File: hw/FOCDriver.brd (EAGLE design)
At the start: 82.5 x 57.8 mm, 99 parts, among them U1 IX4428N, U2 IX4428N, U3 IX4428N, U4 IRF9389TRPBF, U5 IRF9389TRPBF, U6 IRF9389TRPBF, U7 LM27313XMF, U8 LM358N, U9 LM358N

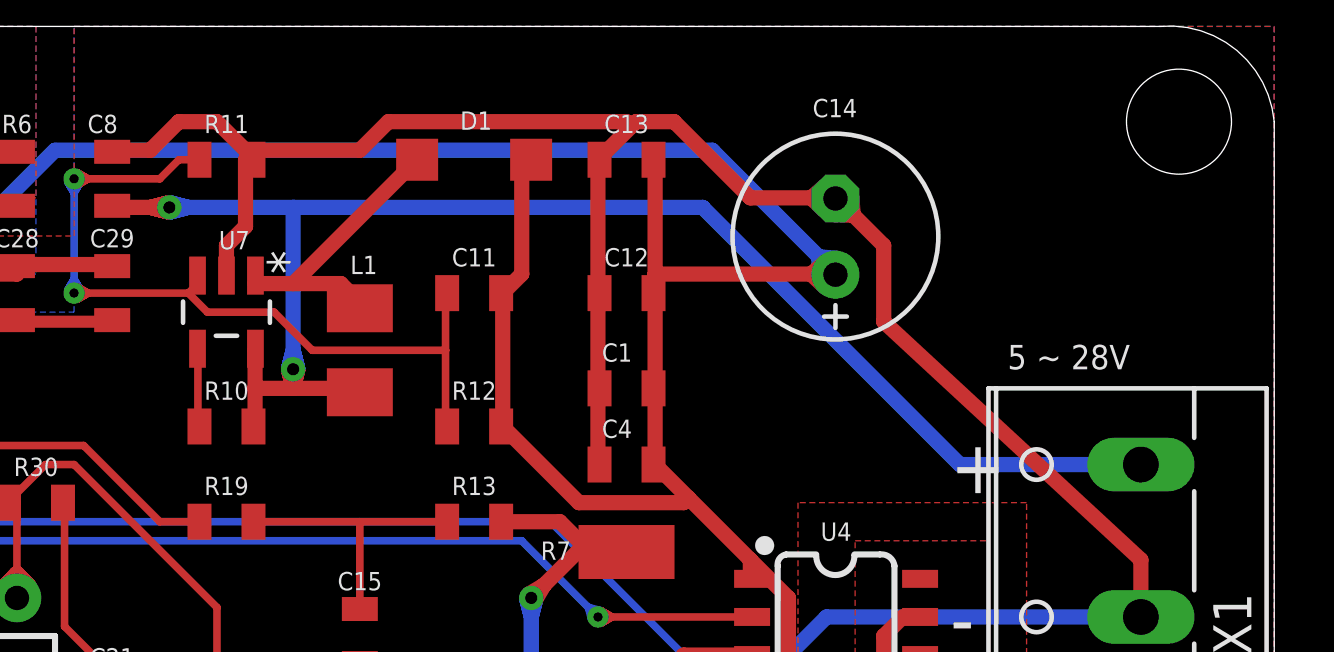
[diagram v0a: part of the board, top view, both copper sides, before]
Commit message: add resettable fuse
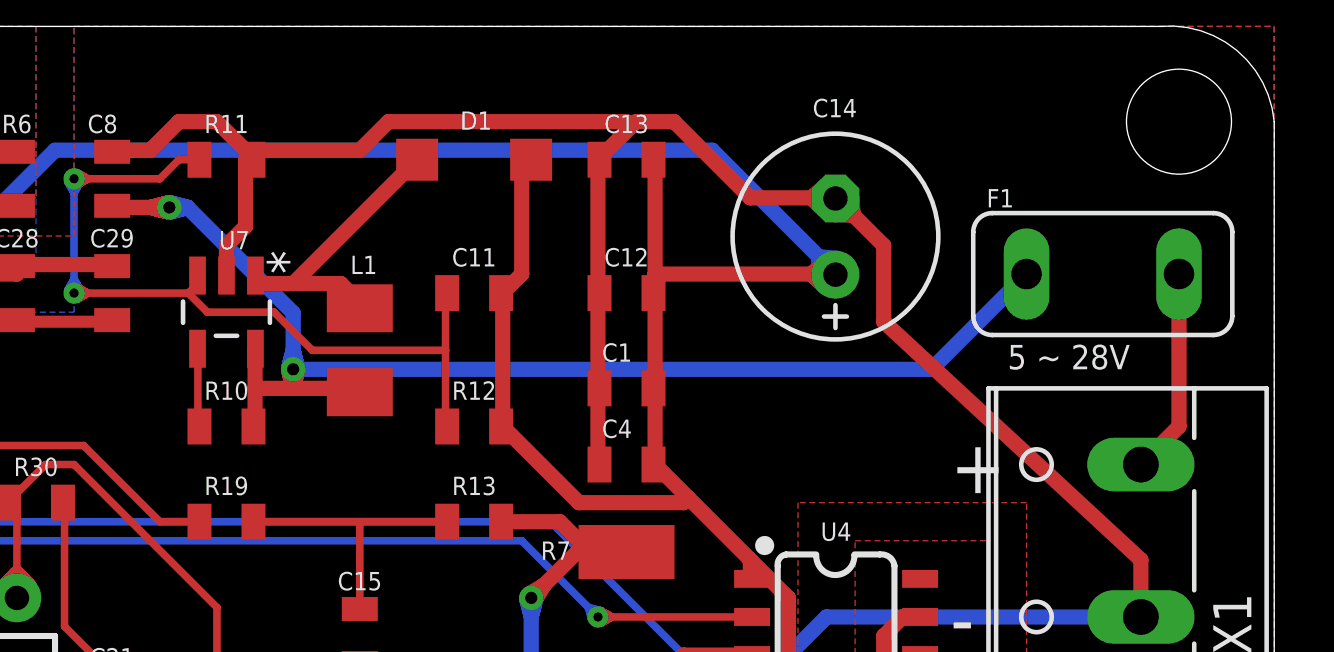
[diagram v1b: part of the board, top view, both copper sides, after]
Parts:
- added F1: 4.00A 16V, fuse:TE5
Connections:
- new net N$27: F1.1, X1.2
- net N$1: now also F1.2; no longer X1.2
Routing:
- net N$1: track 77.5 -> 69.4 mm
- net N$27: track 0.00 -> 6.88 mm
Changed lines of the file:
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@@
 <attribute name="VALUE" x="8.763" y="55.3466" size="1.27" layer="27" ratio="10" rot="R270"/>
 </element>
+<element name="F1" library="fuse" package="TE5" value="4.00A 16V" x="76.835" y="50.8" smashed="yes" rot="R180">
+<attribute name="OC_FARNELL" value="unknown" x="76.835" y="50.8" size="1.778" layer="27" rot="R180" display="off"/>
+<attribute name="MPN" value="" x="76.835" y="50.8" size="1.778" layer="27" rot="R180" display="off"/>
+<attribute name="OC_NEWARK" value="unknown" x="76.835" y="50.8" size="1.778" layer="27" rot="R180" display="off"/>
+<attribute name="MF" value="" x="76.835" y="50.8" size="1.778" layer="27" rot="R180" display="off"/>
+<attribute name="NAME" x="72.9615" y="53.0225" size="0.6096" layer="25" ratio="20"/>
+<attribute name="VALUE" x="81.153" y="54.61" size="1.27" layer="27" ratio="10" rot="R180"/>
+</element>
 </elements>
 <signals>
@@
 <wire x1="45.72" y1="53.0225" x2="45.1104" y2="53.0225" width="0.508" layer="1"/>
 <wire x1="45.1104" y1="53.0225" x2="43.815" y2="53.0225" width="0.508" layer="1"/>
-<wire x1="63.5" y1="53.0225" x2="49.8475" y2="53.0225" width="0.508" layer="16"/>
-<wire x1="49.8475" y1="53.0225" x2="46.3296" y2="53.0225" width="0.508" layer="16"/>
+<wire x1="46.3296" y1="53.0225" x2="49.8475" y2="49.5046" width="0.508" layer="16"/>
+<wire x1="49.8475" y1="49.5046" x2="49.8475" y2="48.2346" width="0.508" layer="16"/>
 <wire x1="46.3296" y1="53.0225" x2="45.72" y2="53.0225" width="0.508" layer="16"/>
-<wire x1="72.0725" y1="44.45" x2="63.5" y2="53.0225" width="0.508" layer="16"/>
-<wire x1="78.105" y1="44.45" x2="72.0725" y2="44.45" width="0.508" layer="16"/>
 <wire x1="43.815" y1="53.0225" x2="43.815" y2="53.075" width="0.508" layer="1"/>
 <wire x1="49.8475" y1="47.625" x2="49.8475" y2="47.0154" width="0.508" layer="1"/>
 <wire x1="49.8475" y1="47.0154" x2="49.8475" y2="46.99" width="0.508" layer="1"/>
-<wire x1="49.8475" y1="53.0225" x2="49.8475" y2="48.2346" width="0.508" layer="16"/>
 <via x="45.72" y="53.0225" extent="1-16" drill="0.4064"/>
 <via x="49.8475" y="47.625" extent="1-16" drill="0.4064"/>
@@
 <wire x1="49.847496875" y1="48.2346" x2="49.6999375" y2="47.663103125" width="0.508" layer="16"/>
 <wire x1="49.6999375" y1="47.663103125" x2="49.6999375" y2="47.6631" width="0.508" layer="16"/>
-<contactref element="X1" pad="2"/>
 <wire x1="45.68189375" y1="52.8749375" x2="45.681896875" y2="52.8749375" width="0.508" layer="1"/>
 <wire x1="46.3296" y1="53.0225" x2="45.758103125" y2="53.170059375" width="0.508" layer="16"/>
@@
 <wire x1="49.847496875" y1="48.2346" x2="49.995059375" y2="47.6631" width="0.508" layer="16"/>
 <wire x1="49.8475" y1="47.625" x2="49.995059375" y2="47.6631" width="0.508" layer="16"/>
+<contactref element="F1" pad="2"/>
+<wire x1="74.295" y1="50.8" x2="71.12" y2="47.625" width="0.508" layer="16"/>
+<wire x1="71.12" y1="47.625" x2="49.8475" y2="47.625" width="0.508" layer="16"/>
 </signal>
 <signal name="N$2">
@@
 <wire x1="3.81" y1="43.815" x2="3.7795375" y2="43.129875" width="0.508" layer="1"/>
 </signal>
+<signal name="N$27" class="3">
+<contactref element="X1" pad="2"/>
+<contactref element="F1" pad="1"/>
+<wire x1="78.105" y1="44.45" x2="79.375" y2="45.72" width="0.508" layer="1"/>
+<wire x1="79.375" y1="45.72" x2="79.375" y2="50.8" width="0.508" layer="1"/>
+</signal>
 </signals>

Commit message: trans
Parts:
- removed C10: 0.1uF, SparkFun-Capacitors:0805
- removed U1, U2, U3: IX4428N, IX4428N:SO08
- added Q1, Q2, Q3, Q4, Q5, Q6: BC546B, transistor-npn:TO92-EBC
- added R47, R50: 330, SparkFun-Resistors:0805
- added R48, R51: 180, SparkFun-Resistors:0805
- added R49: 1K, SparkFun-Resistors:0805
- added R52: 100, SparkFun-Resistors:0805
- C7, C9: value 0.1uF -> 10uF
- R1, R3, R4: value 4.7K -> 1K
- R2: value 4.7K -> 100
- moved C7 128.7 mm to (-11.1, -80.0), turned to 0 degrees
- moved C9 118.4 mm to (-21.6, -80.0), turned to 0 degrees
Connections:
- new net N$28: Q1.E, R48.1
- new net N$30: Q1.B, R1.2
- new net N$32: Q2.B, R49.2
- new net N$39: Q3.B, R3.2
- new net N$40: Q3.E, R51.1
- new net N$41: Q4.B, R4.2
- net +12V: now also R47.2, R50.2; no longer C10.1, U1.6, U2.6, U3.6
- net AGND: no longer C10.2, C7.2, C9.2, U1.3, U2.3, U3.3
- net GND: now also Q2.E, Q4.E, R48.2, R51.2; no longer R1.1, R2.1, R3.1, R4.1
- net N$10: now also C7.2, Q1.C, R47.1; no longer U1.7
- net N$3: no longer U3.5
- net N$6: no longer U3.7
- net N$7: now also Q4.C, R52.2; no longer U2.5
- net N$8: now also C9.2, Q3.C, R50.1; no longer U2.7
- net N$9: now also Q2.C, R2.2; no longer U1.5
- net PWM1H1: now also R1.1, R49.1; no longer R1.2, U1.2
- net PWM1H2: now also R3.1, R4.1; no longer R3.2, U2.2
- net PWM1H3: no longer U3.2
- net PWM1L1: now also R2.1; no longer R2.2, U1.4
- net PWM1L2: now also R52.1; no longer R4.2, U2.4
- net PWM1L3: no longer U3.4
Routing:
- net AGND: track 382.9 -> 376.5 mm
- net N$6: track 63.3 -> 59.9 mm
- net N$8: track 54.5 -> 52.4 mm
- net N$3: track 54.0 -> 51.9 mm
- net +12V: track 205.8 -> 203.9 mm
- net PWM1H1: track 75.8 -> 77.2 mm
- net PWM1L1: track 78.2 -> 79.6 mm
- net N$7: track 65.3 -> 63.9 mm
- net N$10: track 55.6 -> 54.4 mm

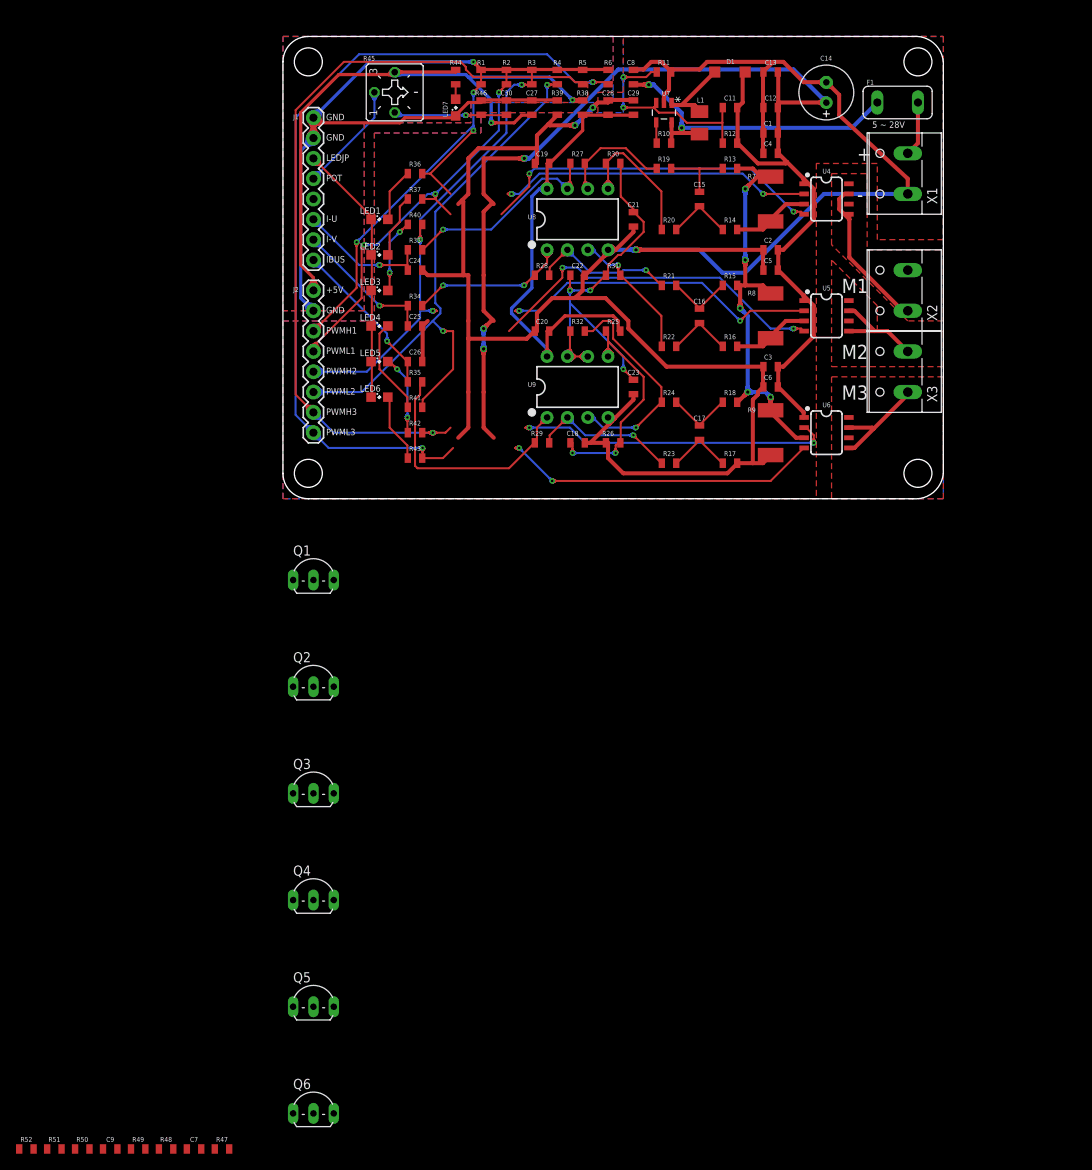
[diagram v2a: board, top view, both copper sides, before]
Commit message: layout trans driver
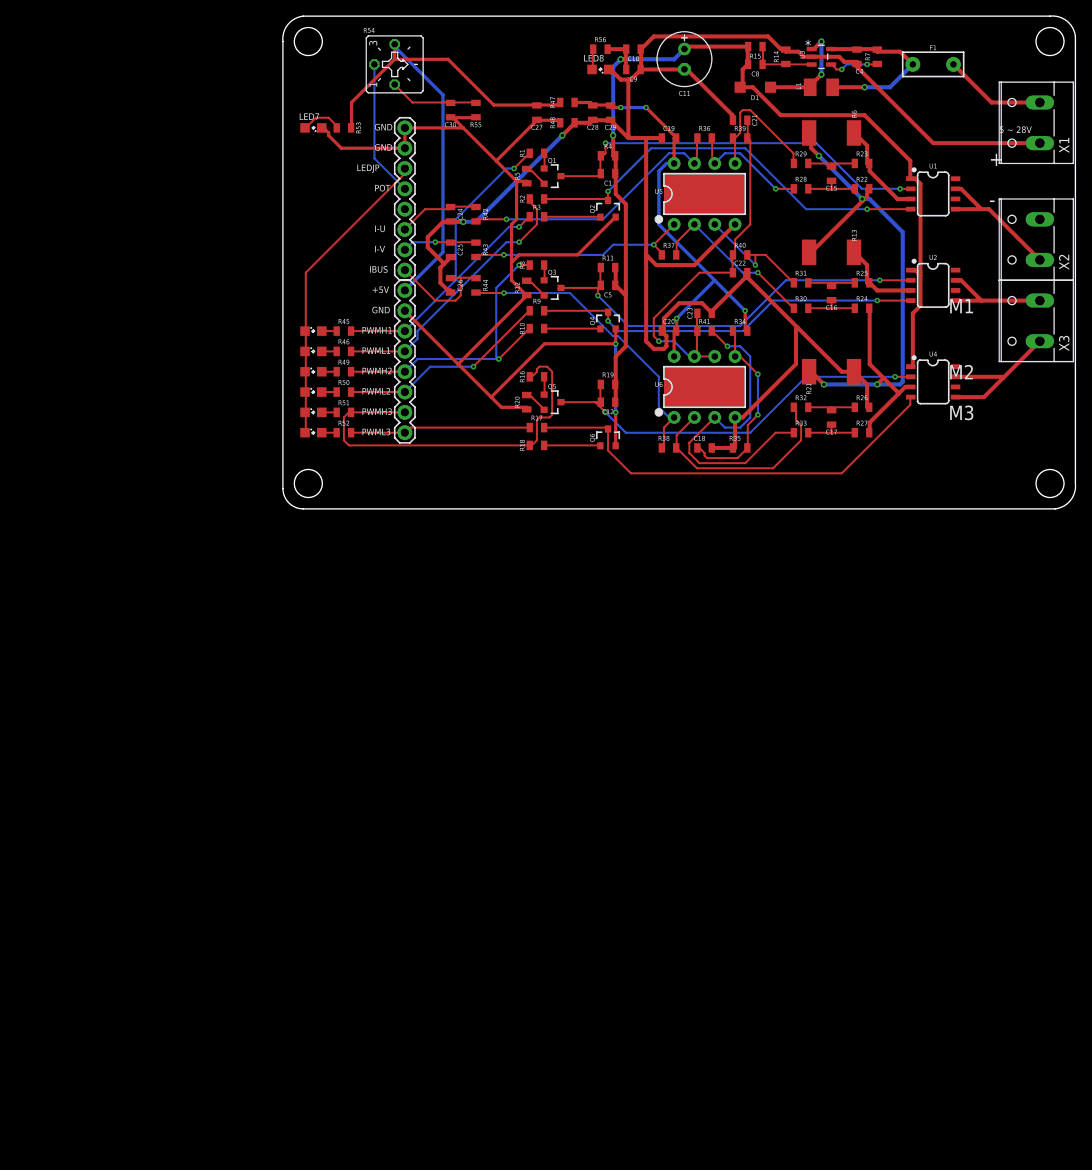
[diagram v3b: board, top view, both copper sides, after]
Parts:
- removed C13: 4.7uF, SparkFun-Capacitors:0805
- removed C14: 470uF, rcl:E2,5-7
- removed C2, C3: 1.0uF, SparkFun-Capacitors:0805
- removed C6: 0.1uF, SparkFun-Capacitors:0805
- removed C7: 10uF, SparkFun-Capacitors:0805
- removed U7: LM27313XMF, LM27313XMF:SOT95P285X120-5N
- removed U8, U9: LM358N, Fairchild-LM358N:DIP08
- added C10: 4.7uF, SparkFun-Capacitors:0805
- added LED8: 12V, led:SML0805
- added R53: 3.3K, SparkFun-Resistors:0805
- added R54: (no value), pot:CT6
- added R55: 1K, SparkFun-Resistors:0805
- added R56: 10K, SparkFun-Resistors:0805
- added U1, U2: IRF9389TRPBF, IRF9389TRPBF:SO08
- added U3: LM27313XMF, LM27313XMF:SOT95P285X120-5N
- C1: value 1.0uF -> 10uF
- C11: value 220pF -> 470uF; device SparkFun-Capacitors:0805 -> rcl:E2,5-7
- C12: value 1nF -> 10uF
- C4, C5: value 0.1uF -> 10uF
- C8: value 10uF -> 220pF
- C9: value 10uF -> 1nF
- F1: value 4.00A 16V -> 16V/4.00A; device fuse:TE5 -> SparkFun-Fuses:PTH
- LED7: value (none) -> 5V
- Q1, Q2, Q3, Q4, Q5, Q6: value BC546B -> BC817; device transistor-npn:TO92-EBC -> SparkFun-DiscreteSemi:SOT23-3
- R10: value 51K -> 1K
- R11: value 13.3K -> 330
- R12: value 118K -> 180
- R13, R21: value 1K 1% -> 0.025R 3W 1%; device SparkFun-Resistors:0805 -> resistor:R2512
- R14: value 1K 1% -> 13.3K
- R15: value 1K 1% -> 118K
- R16, R18: value 1K 1% -> 1K
- R17: value 1K 1% -> 100
- R19: value 1K 1% -> 330
- R20: value 1K 1% -> 180
- R25, R26: value 51K -> 1K 1%
- R27, R28, R29, R30, R31, R32: value 30K 1% -> 1K 1%
- R34, R35: value 1K 1% -> 30K 1%
- R36, R37, R40, R41: value 1K -> 30K 1%
- R38: value 1R -> 30K 1%
- R39: value 0R -> 30K 1%
- R4: value 1K -> 330
- R42, R43: value 1K -> 1K 1%
- R44: value 3.3K -> 1K 1%
- R45: value (none) -> 1K; device pot:CT6 -> SparkFun-Resistors:0805
- R47: value 330 -> 1R
- R48: value 180 -> 0R
- R5: value 4.7K -> 180
- R50: value 330 -> 1K
- R51: value 180 -> 1K
- R52: value 100 -> 1K
- R6: value 4.7K -> 0.025R 3W 1%; device SparkFun-Resistors:0805 -> resistor:R2512
- R7: value 0.025R 3W 1% -> 51K; device resistor:R2512 -> SparkFun-Resistors:0805
- R8: value 0.025R 3W 1% -> 1K; device resistor:R2512 -> SparkFun-Resistors:0805
- R9: value 0.025R 3W 1% -> 100; device resistor:R2512 -> SparkFun-Resistors:0805
- U5, U6: value IRF9389TRPBF -> LM358N; device IRF9389TRPBF:SO08 -> Fairchild-LM358N:DIP08
- moved C9 150.0 mm to (43.8, 54.9)
- moved R47 137.8 mm to (35.6, 50.8)
- moved R48 137.7 mm to (35.6, 48.3)
- moved R49 100.5 mm to (7.62, 17.1)
- moved R50 100.1 mm to (7.62, 14.6)
- moved R51 98.9 mm to (7.62, 12.1)
- moved R52 97.9 mm to (7.62, 9.53)
- moved Q6 91.0 mm to (40.6, 8.89)
- moved Q4 80.1 mm to (40.6, 23.5)
- moved Q5 80.1 mm to (33.7, 13.3), turned to 270 degrees
- moved Q2 69.1 mm to (40.6, 37.5)
- moved Q3 68.7 mm to (33.7, 27.6), turned to 270 degrees
- moved Q1 57.6 mm to (33.7, 41.6), turned to 270 degrees
- moved R33 53.4 mm to (64.8, 9.53)
- moved R27 49.0 mm to (72.4, 9.53)
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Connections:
- removed net PWM1H1: J2.3, R1.1, R36.2, R49.1
- removed net PWM1H2: J2.5, R3.1, R4.1, R40.2
- removed net PWM1H3: J2.7, R42.2, R5.2
- removed net PWM1L1: J2.4, R2.1, R37.2
- removed net PWM1L2: J2.6, R41.2, R52.1
- removed net PWM1L3: J2.8, R43.2, R6.2
- removed net SHUNT_COM: R13.1, R15.1, R18.1, R7.2, R8.2, R9.1, U6.3
- removed net SHUNT_IU: R14.1, R7.1, U4.3
- removed net SHUNT_IV: R16.1, R8.1, U5.3
- new net H1: J2.3, R1.1, R3.1, R45.2
- new net H2: J2.5, R10.1, R49.2, R8.1
- new net H3: J2.7, R16.1, R18.1, R51.2
- new net ICOM: R13.1, R21.1, R22.1, R24.1, R27.1, R6.1, U4.3
- new net IU: R23.1, R6.2, U1.3
- new net IV: R13.2, R25.1, U2.3
- new net L1: J2.4, R2.1, R46.2
- new net L2: J2.6, R50.2, R9.1
- new net L3: J2.8, R17.1, R52.2
- new net N$42: Q5.1, R16.2
- new net N$43: Q3.2, R12.2
- new net N$44: Q6.1, R18.2
- new net N$45: LED8.A, R56.1
- net +12V: now also C10.1, C11.+, C8.2, R11.2, R15.2, R19.2, R4.2, R56.2, U1.1, U2.1; no longer C11.2, C13.1, C14.+, C2.1, C3.1, C4.1, C6.1, C7.1, R12.2, R47.2, R50.2, U5.1, U6.1
- net +5V: now also R47.1, R53.2, R54.E; no longer R38.1, R44.2, R45.E
- net AGND: now also C10.2, C11.-, C9.2, LED8.C, R14.1, R21.2, R35.1, R48.2, U3.2, U5.4, U6.4; no longer C1.2, C12.2, C13.2, C14.-, C2.2, C3.2, C5.2, C6.2, C8.2, R11.1, R17.1, R39.2, R9.2, U7.2, U8.4, U9.4
- net AVDD: now also R34.2, R47.2, U5.8, U6.8; no longer R25.2, R38.2, U8.8, U9.8
- net GND: now also Q2.2, Q4.2, Q6.2, R12.1, R20.1, R48.1, R55.1; no longer Q2.E, Q4.E, R39.1, R46.1, R48.2, R51.2, R6.1
- net IMOTORA: now also R42.2; no longer R33.2
- net IMOTORB: now also R43.2; no longer R34.2
- net IMOTORBUS: now also R44.2; no longer R35.2
- net M1: now also U1.5, U1.7; no longer U4.5, U4.7
- net M2: now also U2.5, U2.7; no longer U5.5, U5.7
- net M3: now also U4.5, U4.7; no longer U6.5, U6.7
- net N$1: now also C4.1, F1.P$2, R7.1, U3.5; no longer C8.1, F1.2, R10.1, U7.5
- net N$10: now also C1.2, Q1.3, R4.1, U1.2; no longer C7.2, Q1.C, R47.1, U4.2
- net N$11: now also R22.2, R28.1; no longer R13.2, R19.1
- net N$12: now also R23.2, R29.1; no longer R14.2, R20.1
- net N$13: now also R28.2, R36.1, U5.6; no longer R19.2, R27.1, U8.6
- net N$14: now also R24.2, R30.1; no longer R15.2, R21.1
- net N$15: now also R29.2, R39.1, U5.5; no longer R20.2, R30.1, U8.5
- net N$16: now also R36.2, R42.1, U5.7; no longer R27.2, R33.1, U8.7
- net N$17: now also R25.2, R31.1; no longer R16.2, R22.1
- net N$18: now also R34.1, R35.2, U6.5; no longer R25.1, R26.2, U9.5
- net N$19: now also R30.2, R37.1, U5.2; no longer R21.2, R28.1, U8.2
- net N$2: now also R7.2, U3.4; no longer R10.2, U7.4
- net N$20: now also R31.2, R40.1, U5.3; no longer R22.2, R31.1, U8.3
- net N$21: now also R37.2, R43.1, U5.1; no longer R28.2, R34.1, U8.1
- net N$22: now also R26.2, R32.1; no longer R17.2, R23.1
- net N$23: now also R27.2, R33.1; no longer R18.2, R24.1
- net N$24: now also R32.2, R38.1, U6.2; no longer R23.2, R29.1, U9.2
- net N$25: now also R33.2, R41.1, U6.3; no longer R24.2, R32.1, U9.3
- net N$26: now also R38.2, R44.1, U6.1; no longer R29.2, R35.1, U9.1
- net N$27: now also F1.P$1; no longer F1.1
- net N$28: now also Q5.2, R20.2; no longer Q1.E, R48.1
- net N$29: now also R54.A, R55.2; no longer R45.A, R46.2
- net N$3: now also Q6.3, R17.2, U4.4; no longer U6.4
- net N$30: now also Q1.1; no longer Q1.B
- net N$31: now also R53.1; no longer R44.1
- net N$32: now also Q2.1, R3.2; no longer Q2.B, R49.2
- net N$33: now also R45.1; no longer R36.1
- net N$34: now also R46.1; no longer R37.1
- net N$35: now also R49.1; no longer R40.1
- net N$36: now also R50.1; no longer R41.1
- net N$37: now also R51.1; no longer R42.1
- net N$38: now also R52.1; no longer R43.1
- net N$39: now also Q3.1, R8.2; no longer Q3.B, R3.2
- net N$4: now also C8.1, R14.2, R15.1, U3.3; no longer C11.1, R11.2, R12.1, U7.3
- net N$40: now also Q1.2, R5.2; no longer Q3.E, R51.1
- net N$41: now also Q4.1, R10.2; no longer Q4.B, R4.2
- net N$5: now also U3.1; no longer U7.1
- net N$6: now also C12.2, Q5.3, R19.1, U4.2; no longer U6.2
- net N$7: now also Q4.3, R9.2, U2.4; no longer Q4.C, R52.2, U5.4
- net N$8: now also C5.2, Q3.3, R11.1, U2.2; no longer C9.2, Q3.C, R50.1, U5.2
- net N$9: now also Q2.3, U1.4; no longer Q2.C, U4.4
- net POT: now also R54.S; no longer R45.S
- net VREF: now also R39.2, R40.2, R41.2, U6.6, U6.7; no longer R30.2, R31.2, R32.2, U9.6, U9.7
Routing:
- net AGND: track 376.5 -> 239.5 mm, vias 3 -> 2
- net PWM1L3: track 131.5 -> 0.00 mm, vias 2 -> 0
- net PWM1H3: track 119.7 -> 0.00 mm, vias 1 -> 0
- net PWM1H2: track 108.3 -> 0.00 mm, vias 3 -> 0
- net SHUNT_COM: track 104.4 -> 0.00 mm, vias 5 -> 0
- net PWM1L2: track 99.9 -> 0.00 mm, vias 2 -> 0
- net ICOM: track 0.00 -> 82.4 mm, vias 0 -> 4
- net PWM1L1: track 79.6 -> 0.00 mm, vias 3 -> 0
- net PWM1H1: track 77.2 -> 0.00 mm, vias 3 -> 0
- net +12V: track 203.9 -> 130.1 mm, vias 3 -> 2
- net VREF: track 111.1 -> 49.2 mm, vias 3 -> 1
- net H3: track 0.00 -> 49.3 mm
- net H1: track 0.00 -> 48.5 mm, vias 0 -> 2
- net N$1: track 69.4 -> 22.5 mm, vias 2 -> 1
- net H2: track 0.00 -> 38.8 mm, vias 0 -> 2
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- removed copper zone on layer 1, net AGND
- removed copper zone on layer 16, net AGND
- removed copper zone on layer 1, net GND
- removed copper zone on layer 16, net GND
- removed copper zone on layer 1, net M1
- removed copper zone on layer 1, net M2
- removed copper zone on layer 1, net M3
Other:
- board size 82.5 x 57.8 mm -> 99.1 x 61.6 mm

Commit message: simulation
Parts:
- added U7, U8, U9: SN74LVC1G17, SN74LVC1G17:SOT23-5
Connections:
- new net N$46: R2.1, U7.4
- new net N$47: R9.1, U8.4
- new net N$48: R17.1, U9.4
- net +5V: now also U7.5, U8.5, U9.5
- net GND: now also U7.3, U8.3, U9.3
- net L1: now also U7.2; no longer R2.1
- net L2: now also U8.2; no longer R9.1
- net L3: now also U9.2; no longer R17.1
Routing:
- net AGND: track 239.5 -> 0.00 mm, vias 2 -> 0
- net GND: track 144.4 -> 0.00 mm, vias 2 -> 0
- net +12V: track 130.1 -> 0.00 mm, vias 2 -> 0
- net ICOM: track 82.4 -> 0.00 mm, vias 4 -> 0
- net +5V: track 71.2 -> 0.00 mm
- net AVDD: track 57.2 -> 0.00 mm, vias 4 -> 0
- net N$3: track 54.4 -> 0.00 mm
- net N$9: track 52.3 -> 0.00 mm, vias 2 -> 0
- net N$8: track 51.9 -> 0.00 mm, vias 2 -> 0
- net N$6: track 51.2 -> 0.00 mm, vias 2 -> 0
- net N$10: track 49.9 -> 0.00 mm, vias 2 -> 0
- net H3: track 49.3 -> 0.00 mm
- net N$7: track 49.2 -> 0.00 mm, vias 2 -> 0
- net VREF: track 49.2 -> 0.00 mm, vias 1 -> 0
- net H1: track 48.5 -> 0.00 mm, vias 2 -> 0
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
